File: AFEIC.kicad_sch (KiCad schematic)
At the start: 39 parts, among them J4 CONN HEADER VERT 6POS 1.5MM, U1 TLE9012DQUXUMA1

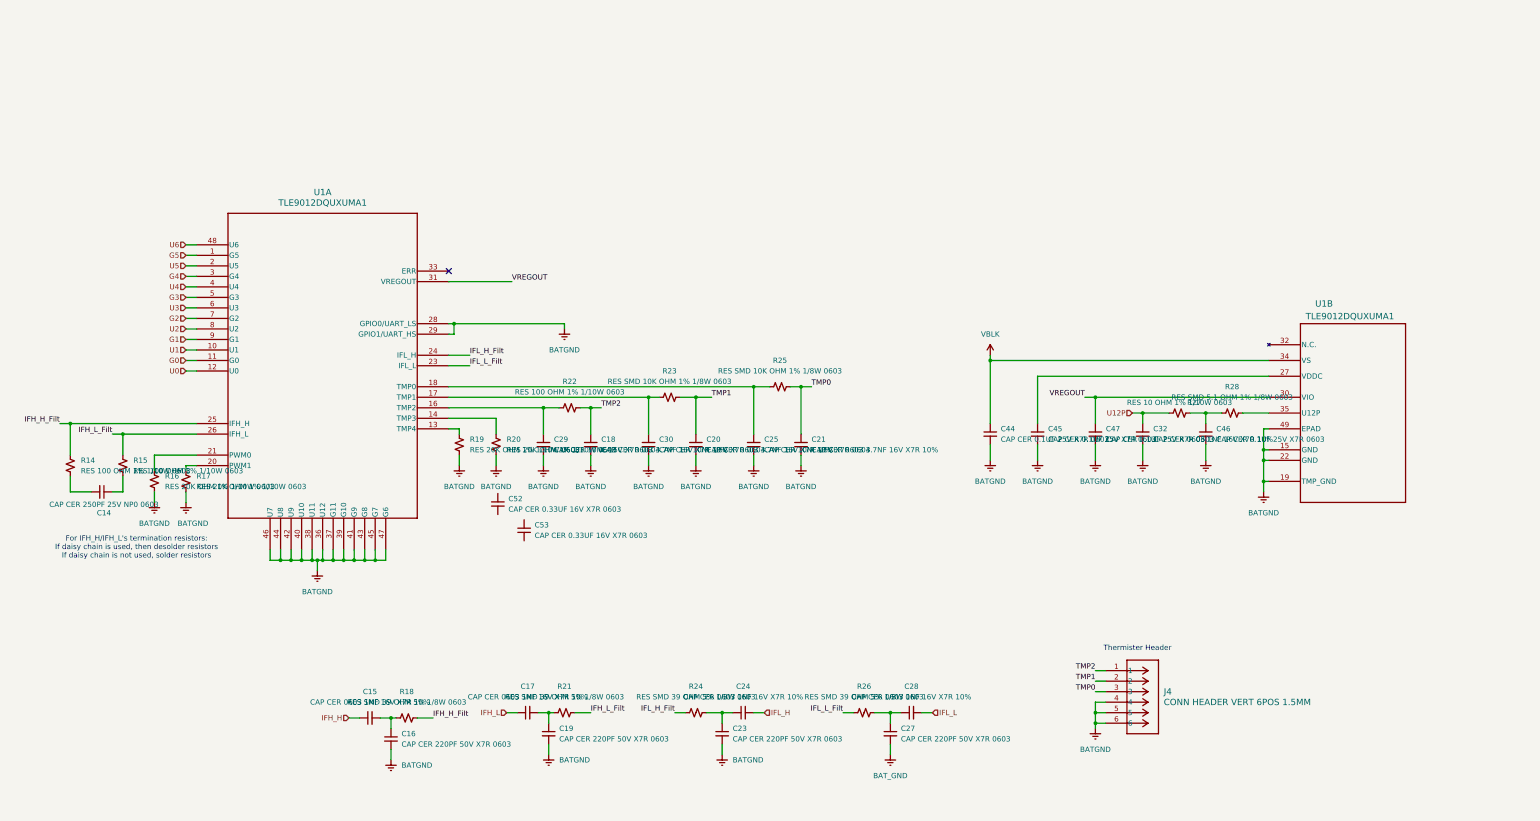
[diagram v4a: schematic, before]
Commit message: cleaned up schematic
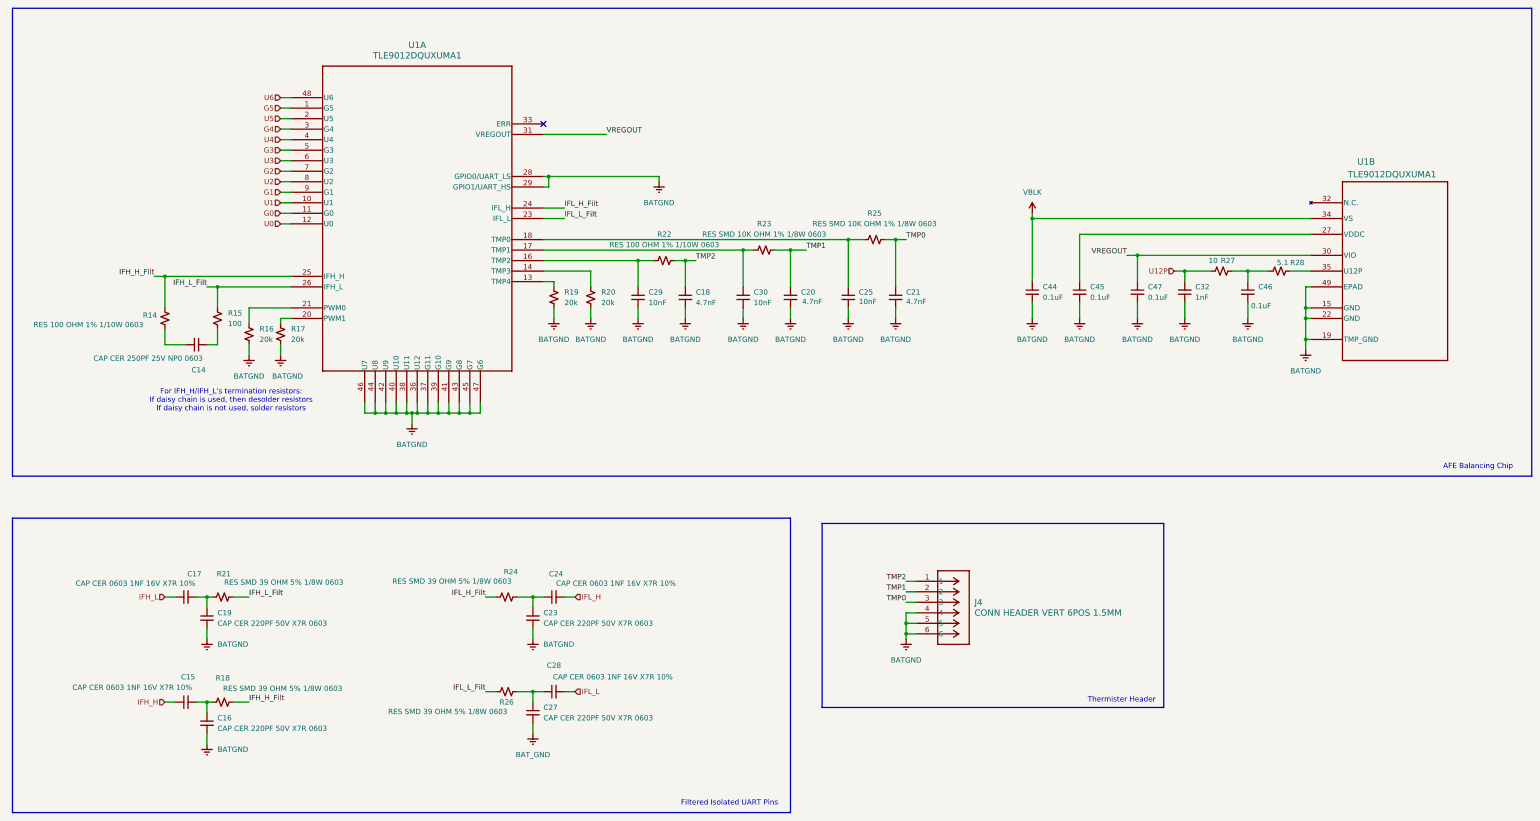
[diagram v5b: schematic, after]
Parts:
- removed C52, C53: CAP CER 0.33UF 16V X7R 0603, Capacitor_SMD:C_0603_1608Metric, symbol Device:C_Small
- C18, C20, C21: value CAP CER 0603 4.7NF 16V X7R 10% -> 4.7nF
- C25, C29, C30: value CAP CER 10NF 16V X7R 0603 -> 10nF
- C32: value CAP CER 0603 1NF 16V X7R 10% -> 1nF
- C44, C45, C46, C47: value CAP CER 0.1UF 25V X7R 0603 -> 0.1uF
- R15: value RES 100 OHM 1% 1/10W 0603 -> 100
- R16, R17, R19, R20: value RES 20K OHM 1% 1/10W 0603 -> 20k
- R27: value RES 10 OHM 1% 1/10W 0603 -> 10
- R28: value RES SMD 5.1 OHM 1% 1/8W 0603 -> 5.1
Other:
- note added: "AFE Balancing Chip"
- note added: "Filtered Isolated UART Pins"
- moved on the sheet: C14, C15, C16, C17, C18, C19, C20, C21, C23, C24, C25, C27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

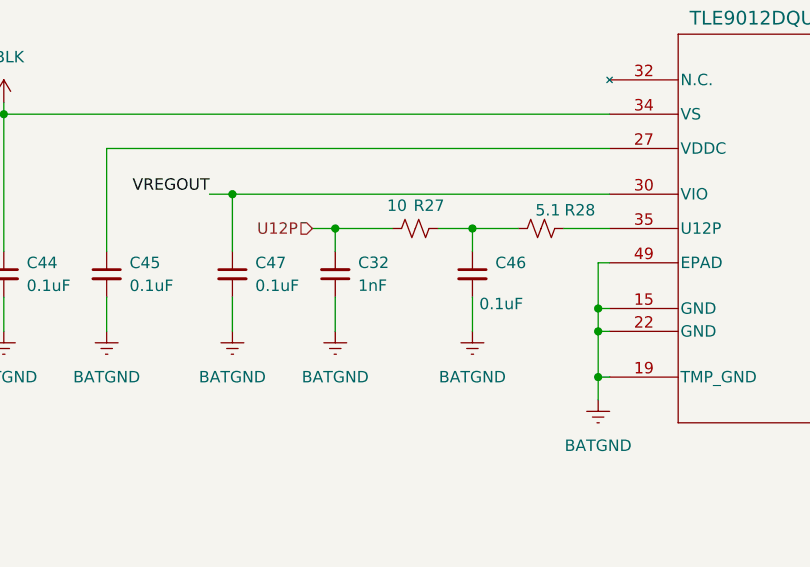
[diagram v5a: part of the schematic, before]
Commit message: fixed capacitor values
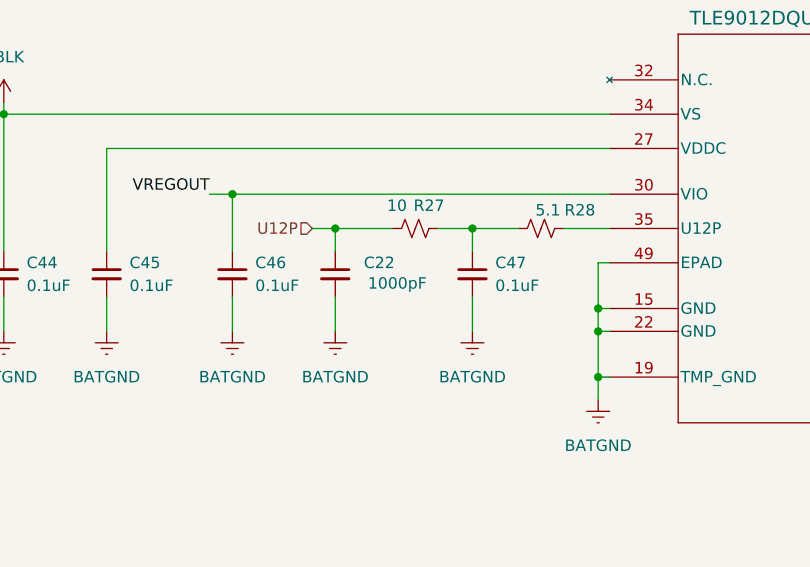
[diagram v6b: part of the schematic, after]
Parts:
- removed C32: 1nF, Capacitor_SMD:C_0603_1608Metric, symbol Device:C_Small
- added C22: 1000pF, Capacitor_SMD:C_0603_1608Metric, symbol Device:C_Small
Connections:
- net BATGND: now also C22.2
- net U12P: now also C22.1
- net VREGOUT: now also C46.1; no longer C47.1
- net at R27.2, R28.1: now also C47.1; no longer C46.1
